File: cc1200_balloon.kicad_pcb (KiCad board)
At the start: 4 copper layers, 50 x 30 mm, 131 parts, among them J101 BATT pads, J201 LoRa ANT pads, J202 SWD+DBG pads, J301 434MHz ANT pads, J401 GNSS ANT pads, J501 BMV080, Q101 DMG3401LSN-7, SW101 PWR, U101 TPS63001, U201 Wio-E5, U301 CC1200, U401 AT6558R-5N32, U501 SCD40-D-R2, U502 AS3935-BQFT, U503 BME688, U504 BME688, X301 40MHz, X401 TCXO 26MHz, X402 32.768kHz

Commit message: Adjust schematic
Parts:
- removed C103, C420, C421: 100n, Capacitor_SMD:C_0402_1005Metric
- removed C105: 10u, Capacitor_SMD:C_0603_1608Metric
- removed C415, C416: 10p, Capacitor_SMD:C_0402_1005Metric
- removed C417, C418, C419: 1u, Capacitor_SMD:C_0402_1005Metric
- removed C422: 100m, cc1200_balloon:SuperCap_KEMET_FCS_D10.7mm
- removed L101: 2.2u, Inductor_SMD:L_1008_2520Metric
- removed R404, R405: 0R, Resistor_SMD:R_0402_1005Metric
- removed U101: TPS63001, Package_SON:VSON-10-1EP_3x3mm_P0.5mm_EP1.65x2.4mm
- added Q102: DMG3401LSN-7, Package_TO_SOT_SMD:SOT-23, F.Cu at (142.4, 111.2)
- C102, C411: value 10u -> 1u; footprint Capacitor_SMD:C_0603_1608Metric -> Capacitor_SMD:C_0402_1005Metric
- C401: value 470p -> 100n
- C402: value 1u -> 100p
- C404, C406: value 100n -> 4u7; footprint Capacitor_SMD:C_0402_1005Metric -> Capacitor_SMD:C_0603_1608Metric
- C405, C412: value 1u -> 100n
- C407, C408, C410: value 100n -> 1u
- C414: value 100p -> 100m; footprint Capacitor_SMD:C_0402_1005Metric -> cc1200_balloon:SuperCap_KEMET_FCS_D10.7mm
- L402: value 4n3 -> 6n8
- R102: value 100R -> 10k
- R402, R403: value 10k -> 22R
- TP401: value GNSS TMS -> GNSS TCK
- TP402: value GNSS TCK -> GNSS TMS
- moved C407 160.7 mm to (235.8, 117.8), turned to 180 degrees
- moved C408 160.2 mm to (235.8, 115.8), turned to 180 degrees
- moved C401 137.0 mm to (255.5, 100.5)
- moved C402 137.0 mm to (255.5, 102.4)
- moved C403 137.0 mm to (255.5, 104.4)
- moved C411 137.0 mm to (247.5, 122.5)
- moved J401 137.0 mm to (214.0, 70.7)
- moved L401 137.0 mm to (230.6, 66.8)
- moved L402 137.0 mm to (230.6, 68.7)
- moved L403 137.0 mm to (247.4, 118.7)
- moved R401 137.0 mm to (230.6, 70.7)
- moved R402 137.0 mm to (230.6, 72.7)
- moved R403 137.0 mm to (230.6, 74.7)
- moved X402 137.0 mm to (243.3, 113.8)
- moved C404 137.0 mm to (247.0, 120.2)
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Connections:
- net /Sensors/AS_ACG renamed Net-(U502-ACG)
- net DBG_TX renamed /MCU/DBG_TX
- net Net-(J201-In) renamed /MCU/LORA_RF
- net Net-(U301-DCPL_PFD_CHP) renamed /CC1200 Radio/CC_DCPL_PFD
- net RADIO_GPIO0 renamed /CC1200 Radio/RADIO_GPIO0
- net RADIO_GPIO3 renamed /CC1200 Radio/RADIO_GPIO3
- net RF_LNAN renamed /CC1200 Radio/RF_LNAN
- net RF_LNAP renamed /CC1200 Radio/RF_LNAP
- net RF_PA renamed /CC1200 Radio/RF_PA
- net RF_TRXSW renamed /CC1200 Radio/RF_TRXSW
- net STATUS_LED renamed /MCU/STATUS_LED
- net SWCLK renamed /MCU/SWCLK
- net SWDIO renamed /MCU/SWDIO
- net XOSC_Q1 renamed /CC1200 Radio/XOSC_Q1
- net XOSC_Q2 renamed /CC1200 Radio/XOSC_Q2
- C102 pad 1: VBATT -> /Power/PWR_GATE
- C102 pad 2: GND -> VBATT
- C104 pad 1: +3V3 -> +BATT
- C106 pad 1: +3V3 -> +BATT
- C201 pad 1: +3V3 -> +BATT
- C202 pad 1: +3V3 -> +BATT
- C203 pad 1: +3V3 -> +BATT
- C301 pad 1: +3V3 -> +BATT
- C302 pad 1: +3V3 -> +BATT
- C303 pad 1: +3V3 -> +BATT
- C304 pad 1: +3V3 -> +BATT
- C305 pad 1: +3V3 -> +BATT
- C306 pad 1: +3V3 -> +BATT
- C307 pad 1: +3V3 -> +BATT
- C308 pad 1: +3V3 -> +BATT
- C309 pad 1: +3V3 -> +BATT
- C310 pad 1: +3V3 -> +BATT
- C311 pad 1: +3V3 -> +BATT
- C312 pad 1: +3V3 -> +BATT
- C320 pad 1: +3V3 -> +BATT
- C401 pad 1: /GNSS/GNSS_ANT_FEED -> /GNSS/GNSS_ANT_BIAS
- C401 pad 2: Net-(C401-Pad2) -> GND
- C402 pad 1: GNSS_ANT_BIAS -> /GNSS/GNSS_ANT_FEED
- C402 pad 2: GND -> Net-(C402-Pad2)
- C403 pad 1: +3V3 -> +BATT
- C404 pad 1: GNSS_VDX -> +BATT
- C405 pad 1: GNSS_AVDD -> +BATT
- C406 pad 1: GNSS_V1P2BB -> /GNSS/GNSS_VCORE
- C407 pad 1: +3V3 -> /GNSS/GNSS_VDD_ANA
- C408 pad 1: +3V3 -> /GNSS/GNSS_VDD12BK
- C409 pad 1: GNSS_V1P2BB -> /GNSS/GNSS_VDD12BB
- C410 pad 1: +3V3 -> /GNSS/GNSS_VDD_PLL
- C411 pad 1: GNSS_VDX -> /GNSS/GNSS_VDD_RF
- C412 pad 1: GNSS_VDD12BK -> /GNSS/GNSS_VX
- C413 pad 1: +3V3 -> /GNSS/GNSS_VBCKP
- C414 pad 1: Net-(X401-OUT) -> /GNSS/GNSS_VBCKP
- C414 pad 2: GNSS_XREF -> GND
- C501 pad 1: +3V3 -> +BATT
- C502 pad 1: +3V3 -> +BATT
- C504 pad 1: +3V3 -> +BATT
- C507 pad 1: +3V3 -> +BATT
- C508 pad 1: +3V3 -> +BATT
- C509 pad 1: +3V3 -> +BATT
- C510 pad 1: +3V3 -> +BATT
- C511 pad 1: +3V3 -> +BATT
- C512 pad 1: +3V3 -> +BATT
- C513 pad 1: +3V3 -> +BATT
- C514 pad 1: +3V3 -> +BATT
- J202 pad 1: +3V3 -> +BATT
- J501 pad 1: +3V3 -> +BATT
- J501 pad 10: +3V3 -> +BATT
- J501 pad 3: +3V3 -> +BATT
- J501 pad 8: +3V3 -> +BATT
- L401 pad 2: GNSS_ANT_BIAS -> /GNSS/GNSS_ANT_BIAS
- L402 pad 1: Net-(C401-Pad2) -> Net-(C402-Pad2)
- L402 pad 2: GNSS_LNA_IN -> /GNSS/GNSS_RF_IN
- L403 pad 1: GNSS_DCDC_SW -> /GNSS/GNSS_DX_SW
- L403 pad 2: GNSS_VDX -> /GNSS/GNSS_VCORE
- R101 pad 1: EN_3V3 -> /Power/PWR_GATE
- R101 pad 2: GND -> VBATT
- R102 pad 1: VBATT -> /Power/SW_ON
- R102 pad 2: /Power/VINA -> /Power/PWR_GATE
- R103 pad 1: VBATT -> +BATT
- R201 pad 1: +3V3 -> +BATT
- R203 pad 1: +3V3 -> +BATT
- R204 pad 1: +3V3 -> +BATT
- R302 pad 1: +3V3 -> +BATT
- R401 pad 1: GNSS_TXD_RAW -> /GNSS/GNSS_TEST
- R401 pad 2: GNSS_TX -> GND
- R402 pad 1: GNSS_RXD_RAW -> /GNSS/GNSS_TXD_RAW
- R402 pad 2: GNSS_RX -> GNSS_TX
- R403 pad 1: GNSS_TEST -> /GNSS/GNSS_RXD_RAW
- R403 pad 2: GND -> GNSS_RX
- SW101 pad 2: EN_3V3 -> /Power/SW_ON
- TP401 pad 1: GNSS_TMS -> /GNSS/GNSS_TCK
- TP402 pad 1: GNSS_TCK -> /GNSS/GNSS_TMS
- U201 pad 1: +3V3 -> +BATT
- U301 pad 1: +3V3 -> +BATT
- U301 pad 12: +3V3 -> +BATT
- U301 pad 13: +3V3 -> +BATT
- U301 pad 15: +3V3 -> +BATT
- U301 pad 22: +3V3 -> +BATT
- U301 pad 25: +3V3 -> +BATT
- U301 pad 27: +3V3 -> +BATT
- U301 pad 28: +3V3 -> +BATT
- U301 pad 5: +3V3 -> +BATT
- U401 pad 1: GNSS_LNA_IN -> /GNSS/GNSS_VDD_ANA
- U401 pad 10: unconnected-(U401-GPIO9-Pad10) -> /GNSS/GNSS_ANT_BIAS
- U401 pad 11: unconnected-(U401-GPIO2/SCL-Pad11) -> /GNSS/GNSS_RTC_O
- U401 pad 12: unconnected-(U401-GPIO3/SDA-Pad12) -> /GNSS/GNSS_RTC_I
- U401 pad 13: GNSS_V1P2BB -> unconnected-(U401-GPIO4/TXD1-Pad13)
- U401 pad 14: +3V3 -> unconnected-(U401-GPIO5/RXD1-Pad14)
- U401 pad 15: unconnected-(U401-GPIO4/TXD2-Pad15) -> /GNSS/GNSS_TCK
- U401 pad 16: unconnected-(U401-GPIO5/RXD2-Pad16) -> /GNSS/GNSS_TMS
- U401 pad 17: GNSS_TMS -> unconnected-(U401-nRST-Pad17)
- U401 pad 18: GNSS_TCK -> /GNSS/GNSS_RXD_RAW
- U401 pad 19: GNSS_TXD_RAW -> /GNSS/GNSS_TXD_RAW
- U401 pad 2: GNSS_ANT_BIAS -> /GNSS/GNSS_VX
- U401 pad 20: GNSS_RXD_RAW -> unconnected-(U401-GPIO6-Pad20)
- U401 pad 21: GNSS_PPS -> +BATT
- U401 pad 22: +3V3 -> /GNSS/GNSS_DX_SW
- U401 pad 23: NRST -> /GNSS/GNSS_VCORE
- U401 pad 24: GNSS_V1P2BB -> /GNSS/GNSS_VDD12BB
- U401 pad 25: GNSS_VDX -> unconnected-(U401-NC-Pad25)
- U401 pad 26: GNSS_DCDC_SW -> unconnected-(U401-NC-Pad26)
- U401 pad 27: +3V3 -> unconnected-(U401-NC-Pad27)
- U401 pad 28: GNSS_TEST -> unconnected-(U401-NC-Pad28)
- U401 pad 29: GNSS_ONOFF -> /GNSS/GNSS_TEST
- U401 pad 3: +3V3 -> /GNSS/GNSS_XREF
- U401 pad 30: GNSS_XREF -> GNSS_ONOFF
- U401 pad 31: GNSS_VBK -> unconnected-(U401-GPIO10/SCL-Pad31)
- U401 pad 32: GNSS_VDD12BK -> unconnected-(U401-GPIO11/SDA-Pad32)
- U401 pad 33: GNSS_RTC_XO -> unconnected-(U401-GPIO16-Pad33)
- U401 pad 34: GNSS_RTC_XI -> unconnected-(U401-GPIO12-Pad34)
- U401 pad 35: GNSS_VDX -> GNSS_PPS
- U401 pad 36: GNSS_DVDD -> unconnected-(U401-GPIO14-Pad36)
- U401 pad 37: GNSS_VDD_PLL -> unconnected-(U401-GPIO15-Pad37)
- U401 pad 38: unconnected-(U401-RFA_IN-Pad38) -> /GNSS/GNSS_VDD_PLL
- U401 pad 39: GNSS_VDD_RF -> /GNSS/GNSS_VDD_RF
- U401 pad 4: GNSS_VDX -> unconnected-(U401-TST_RF-Pad4)
- U401 pad 40: unconnected-(U401-LNA_OUT-Pad40) -> /GNSS/GNSS_RF_IN
- U401 pad 5: unconnected-(U401-TST_ANA-Pad5) -> /GNSS/GNSS_VDD12BK
- U401 pad 6: GNSS_AVDD -> /GNSS/GNSS_VBCKP
- U401 pad 7: unconnected-(U401-TST_DIG-Pad7) -> +BATT
- U501 pad 19: +3V3 -> +BATT
- U501 pad 7: +3V3 -> +BATT
- U502 pad 15: +3V3 -> +BATT
- U502 pad 16: +3V3 -> +BATT
- U502 pad 5: +3V3 -> +BATT
- U502 pad 6: +3V3 -> +BATT
- U502 pad 8: +3V3 -> +BATT
- U502 pad 9: +3V3 -> +BATT
- U503 pad 2: +3V3 -> +BATT
- U503 pad 6: +3V3 -> +BATT
- U503 pad 8: +3V3 -> +BATT
- U504 pad 2: +3V3 -> +BATT
- U504 pad 5: +3V3 -> +BATT
- U504 pad 6: +3V3 -> +BATT
- U504 pad 8: +3V3 -> +BATT
- X401 pad 1: Net-(X401-Tri-State) -> /GNSS/GNSS_VX
- X401 pad 3: Net-(X401-OUT) -> /GNSS/GNSS_XREF
- X401 pad 4: +3V3 -> /GNSS/GNSS_VX
- X402 pad 1: GNSS_RTC_XI -> /GNSS/GNSS_RTC_I
- X402 pad 2: GNSS_RTC_XO -> /GNSS/GNSS_RTC_O
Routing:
- added copper zone on In2.Cu, net +BATT
- removed copper zone on In2.Cu, net +3V3

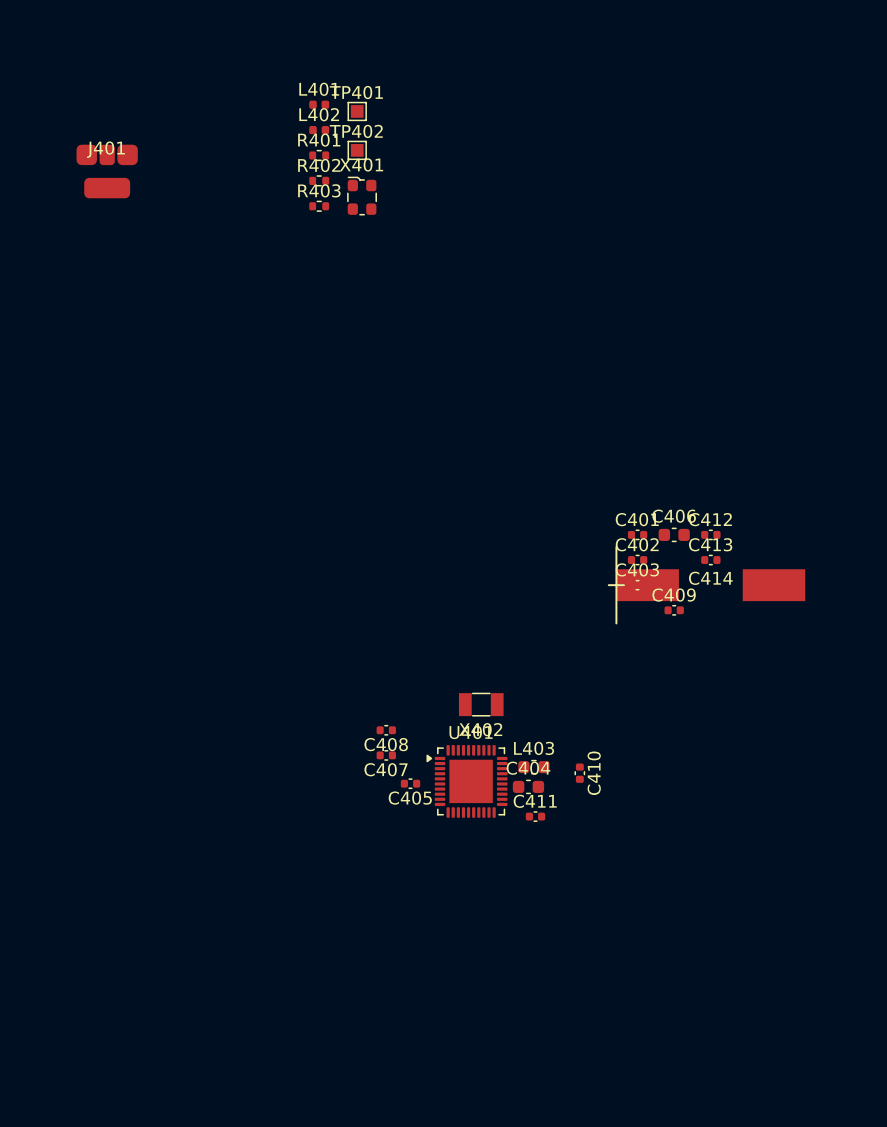
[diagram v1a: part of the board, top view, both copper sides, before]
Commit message: Update schematic wiring
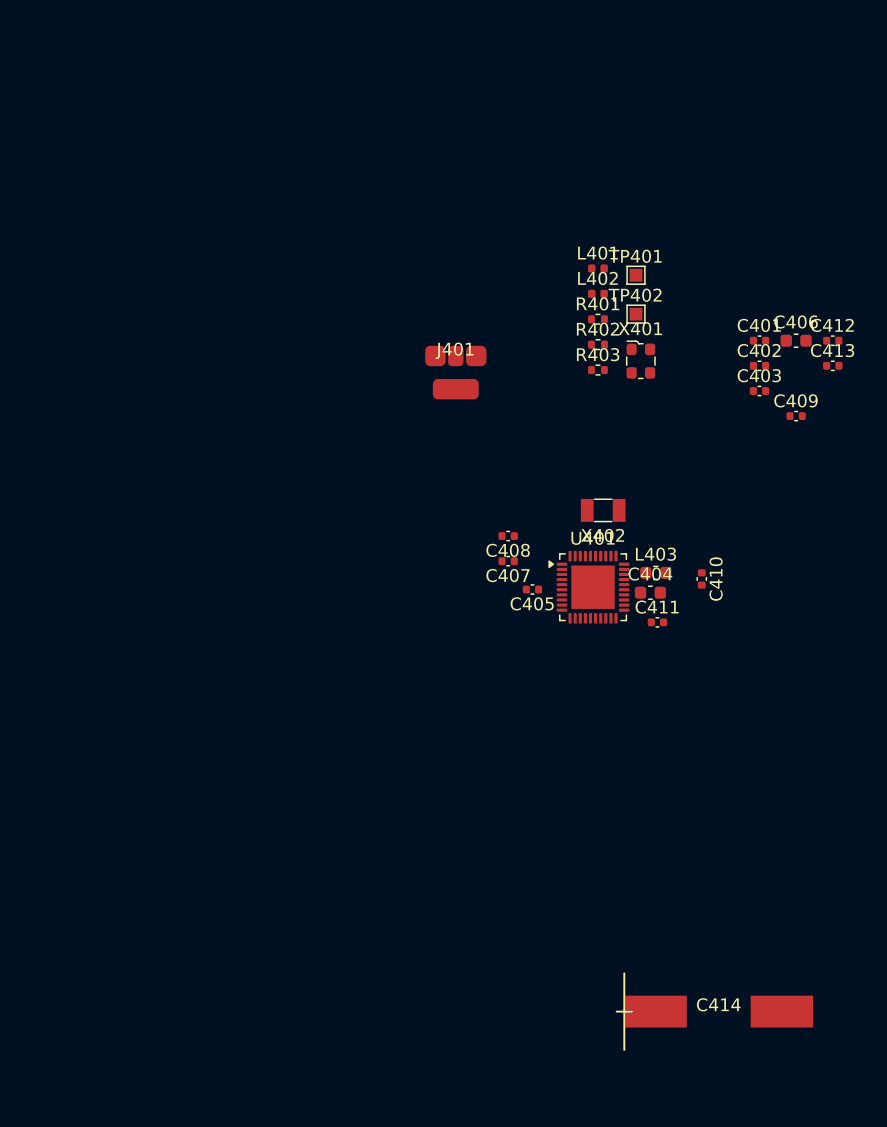
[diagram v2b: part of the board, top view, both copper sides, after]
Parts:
- moved C414 33.4 mm to (261.9, 137.8)
- moved J401 31.5 mm to (241.3, 86.5)
- moved X401 25.3 mm to (255.8, 86.8)
- moved L401 25.3 mm to (252.4, 79.6)
- moved R402 25.3 mm to (252.4, 85.6)
- moved TP401 25.3 mm to (255.4, 80.1)
- moved TP402 25.3 mm to (255.4, 83.2)
- moved L402 25.3 mm to (252.4, 81.6)
- moved R401 25.3 mm to (252.4, 83.6)
- moved R403 25.3 mm to (252.4, 87.5)
- moved C401 18.0 mm to (265.1, 85.2)
- moved C402 18.0 mm to (265.1, 87.2)
- moved C403 18.0 mm to (265.1, 89.2)
- moved C411 18.0 mm to (257.1, 107.3)
- moved L403 18.0 mm to (257.0, 103.5)
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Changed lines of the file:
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@@
 	(footprint "cc1200_balloon:AT6558R_QFN-40-1EP_5x5mm_P0.4mm_EP3.4x3.4mm"
 		(layer "F.Cu")
-		(at 242.5 119.79)
+		(at 252.055 104.57)
 		(descr "QFN, 40 pin, 5x5mm body, 0.4mm pitch, 3.4x3.4mm thermal pad (ZHONGKEWEI AT6558R data sheet section 8.2)")
 		(tags "QFN NoLead")
@@
 	(footprint "Inductor_SMD:L_0603_1608Metric"
 		(layer "F.Cu")
-		(at 247.42 118.67)
+		(at 256.975 103.45)
 		(descr "Inductor SMD 0603 (1608 Metric), square (rectangular) end terminal, IPC-7351 nominal, (Body size source: http://www.tortai-tech.com/upload/download/2011102023233369053.pdf)")
 		(tags "inductor")
@@
 	(footprint "Inductor_SMD:L_0402_1005Metric"
 		(layer "F.Cu")
-		(at 230.5925 66.755)
+		(at 252.44 79.59)
 		(descr "Inductor SMD 0402 (1005 Metric), square (rectangular) end terminal, IPC-7351 nominal, (Body size source: http://www.tortai-tech.com/upload/download/2011102023233369053.pdf)")
 		(tags "inductor")
@@
 	(footprint "cc1200_balloon:SuperCap_KEMET_FCS_D10.7mm"
 		(layer "F.Cu")
-		(at 261.285 104.41)
+		(at 261.905 137.83)
 		(descr "KEMET FC/FCS series supercapacitor, 10.7mm diameter SMD can, 5.5mm high; pad 1 is positive")
 		(tags "supercapacitor EDLC backup KEMET")
@@
 	(footprint "Capacitor_SMD:C_0402_1005Metric"
 		(layer "F.Cu")
-		(at 258.415 106.38)
+		(at 267.97 91.16)
 		(descr "Capacitor SMD 0402 (1005 Metric), square (rectangular) end terminal, IPC-7351 nominal, (Body size source: IPC-SM-782 page 76, https://www.pcb-3d.com/wordpress/wp-content/uploads/ipc-sm-782a_amendment_1_and_2.pdf)")
 		(tags "capacitor")
@@
 	(footprint "TestPoint:TestPoint_Pad_1.0x1.0mm"
 		(layer "F.Cu")
-		(at 233.5725 67.285)
+		(at 255.42 80.12)
 		(descr "SMD rectangular pad as test Point, square 1.0mm side length")
 		(tags "test point SMD pad rectangle square")
@@
 	(footprint "Capacitor_SMD:C_0402_1005Metric"
 		(layer "F.Cu")
-		(at 255.545 100.47)
+		(at 265.1 85.25)
 		(descr "Capacitor SMD 0402 (1005 Metric), square (rectangular) end terminal, IPC-7351 nominal, (Body size source: IPC-SM-782 page 76, https://www.pcb-3d.com/wordpress/wp-content/uploads/ipc-sm-782a_amendment_1_and_2.pdf)")
 		(tags "capacitor")
@@
 	(footprint "Capacitor_SMD:C_0402_1005Metric"
 		(layer "F.Cu")
-		(at 261.285 100.47)
+		(at 270.84 85.25)
 		(descr "Capacitor SMD 0402 (1005 Metric), square (rectangular) end terminal, IPC-7351 nominal, (Body size source: IPC-SM-782 page 76, https://www.pcb-3d.com/wordpress/wp-content/uploads/ipc-sm-782a_amendment_1_and_2.pdf)")
 		(tags "capacitor")
@@
 	(footprint "Capacitor_SMD:C_0402_1005Metric"
 		(layer "F.Cu")
-		(at 235.85 117.75 180)
+		(at 245.405 102.53 180)
 		(descr "Capacitor SMD 0402 (1005 Metric), square (rectangular) end terminal, IPC-7351 nominal, (Body size source: IPC-SM-782 page 76, https://www.pcb-3d.com/wordpress/wp-content/uploads/ipc-sm-782a_amendment_1_and_2.pdf)")
 		(tags "capacitor")
@@
 	(footprint "Capacitor_SMD:C_0603_1608Metric"
 		(layer "F.Cu")
-		(at 246.995 120.22)
+		(at 256.55 105)
 		(descr "Capacitor SMD 0603 (1608 Metric), square (rectangular) end terminal, IPC-7351 nominal, (Body size source: IPC-SM-782 page 76, https://www.pcb-3d.com/wordpress/wp-content/uploads/ipc-sm-782a_amendment_1_and_2.pdf)")
 		(tags "capacitor")
@@
 	(footprint "Capacitor_SMD:C_0402_1005Metric"
 		(layer "F.Cu")
-		(at 261.285 102.44)
+		(at 270.84 87.22)
 		(descr "Capacitor SMD 0402 (1005 Metric), square (rectangular) end terminal, IPC-7351 nominal, (Body size source: IPC-SM-782 page 76, https://www.pcb-3d.com/wordpress/wp-content/uploads/ipc-sm-782a_amendment_1_and_2.pdf)")
 		(tags "capacitor")
@@
 	(footprint "Crystal:Crystal_SMD_3215-2Pin_3.2x1.5mm"
 		(layer "F.Cu")
-		(at 243.295 113.77 180)
+		(at 252.85 98.55 180)
 		(descr "SMD Crystal FC-135 https://support.epson.biz/td/api/doc_check.php?dl=brief_FC-135R_en.pdf")
 		(tags "SMD SMT Crystal")
@@
 	(footprint "Resistor_SMD:R_0402_1005Metric"
 		(layer "F.Cu")
-		(at 230.5925 74.715)
+		(at 252.44 87.55)
 		(descr "Resistor SMD 0402 (1005 Metric), square (rectangular) end terminal, IPC-7351 nominal, (Body size source: IPC-SM-782 page 72, https://www.pcb-3d.com/wordpress/wp-content/uploads/ipc-sm-782a_amendment_1_and_2.pdf)")
 		(tags "resistor")
@@
 	(footprint "cc1200_balloon:SolderPad_Coax_Pigtail"
 		(layer "F.Cu")
-		(at 213.9775 70.69)
+		(at 241.3 86.45)
 		(descr "Coax pigtail solder pads: centre conductor, coplanar grounds and a braid pad; replaces an SMA or u.FL connector")
 		(tags "solder pad coax pigtail RF antenna")
@@
 	(footprint "Capacitor_SMD:C_0603_1608Metric"
 		(layer "F.Cu")
-		(at 258.415 100.47)
+		(at 267.97 85.25)
 		(descr "Capacitor SMD 0603 (1608 Metric), square (rectangular) end terminal, IPC-7351 nominal, (Body size source: IPC-SM-782 page 76, https://www.pcb-3d.com/wordpress/wp-content/uploads/ipc-sm-782a_amendment_1_and_2.pdf)")
 		(tags "capacitor")
@@
 	(footprint "Capacitor_SMD:C_0402_1005Metric"
 		(layer "F.Cu")
-		(at 255.545 102.44)
+		(at 265.1 87.22)
 		(descr "Capacitor SMD 0402 (1005 Metric), square (rectangular) end terminal, IPC-7351 nominal, (Body size source: IPC-SM-782 page 76, https://www.pcb-3d.com/wordpress/wp-content/uploads/ipc-sm-782a_amendment_1_and_2.pdf)")
 		(tags "capacitor")
@@
 	(footprint "Capacitor_SMD:C_0402_1005Metric"
 		(layer "F.Cu")
-		(at 251.02 119.145 -90)
+		(at 260.575 103.925 -90)
 		(descr "Capacitor SMD 0402 (1005 Metric), square (rectangular) end terminal, IPC-7351 nominal, (Body size source: IPC-SM-782 page 76, https://www.pcb-3d.com/wordpress/wp-content/uploads/ipc-sm-782a_amendment_1_and_2.pdf)")
 		(tags "capacitor")
@@
 	(footprint "Oscillator:Oscillator_SMD_ECS_2520MV-xxx-xx-4Pin_2.5x2.0mm"
 		(layer "F.Cu")
-		(at 233.9525 74.015)
+		(at 255.8 86.85)
 		(descr "Miniature Crystal Clock Oscillator ECS 2520MV series, https://www.ecsxtal.com/store/pdf/ECS-2520MV.pdf")
 		(tags "Miniature Crystal Clock Oscillator ECS 2520MV series SMD SMT HCMOS")
@@
 	(footprint "Resistor_SMD:R_0402_1005Metric"
 		(layer "F.Cu")
-		(at 230.5925 72.725)
+		(at 252.44 85.56)
 		(descr "Resistor SMD 0402 (1005 Metric), square (rectangular) end terminal, IPC-7351 nominal, (Body size source: IPC-SM-782 page 72, https://www.pcb-3d.com/wordpress/wp-content/uploads/ipc-sm-782a_amendment_1_and_2.pdf)")
 		(tags "resistor")
@@
 	(footprint "Capacitor_SMD:C_0402_1005Metric"
 		(layer "F.Cu")
-		(at 237.75 119.97 180)
+		(at 247.305 104.75 180)
 		(descr "Capacitor SMD 0402 (1005 Metric), square (rectangular) end terminal, IPC-7351 nominal, (Body size source: IPC-SM-782 page 76, https://www.pcb-3d.com/wordpress/wp-content/uploads/ipc-sm-782a_amendment_1_and_2.pdf)")
 		(tags "capacitor")
@@
 	(footprint "Capacitor_SMD:C_0402_1005Metric"
 		(layer "F.Cu")
-		(at 255.545 104.41)
+		(at 265.1 89.19)
 		(descr "Capacitor SMD 0402 (1005 Metric), square (rectangular) end terminal, IPC-7351 nominal, (Body size source: IPC-SM-782 page 76, https://www.pcb-3d.com/wordpress/wp-content/uploads/ipc-sm-782a_amendment_1_and_2.pdf)")
 		(tags "capacitor")
@@
 	(footprint "Inductor_SMD:L_0402_1005Metric"
 		(layer "F.Cu")
-		(at 230.5925 68.745)
+		(at 252.44 81.58)
 		(descr "Inductor SMD 0402 (1005 Metric), square (rectangular) end terminal, IPC-7351 nominal, (Body size source: http://www.tortai-tech.com/upload/download/2011102023233369053.pdf)")
 		(tags "inductor")
@@
 	(footprint "Capacitor_SMD:C_0402_1005Metric"
 		(layer "F.Cu")
-		(at 235.85 115.78 180)
+		(at 245.405 100.56 180)
 		(descr "Capacitor SMD 0402 (1005 Metric), square (rectangular) end terminal, IPC-7351 nominal, (Body size source: IPC-SM-782 page 76, https://www.pcb-3d.com/wordpress/wp-content/uploads/ipc-sm-782a_amendment_1_and_2.pdf)")
 		(tags "capacitor")
@@
 	(footprint "Capacitor_SMD:C_0402_1005Metric"
 		(layer "F.Cu")
-		(at 247.545 122.545)
+		(at 257.1 107.325)
 		(descr "Capacitor SMD 0402 (1005 Metric), square (rectangular) end terminal, IPC-7351 nominal, (Body size source: IPC-SM-782 page 76, https://www.pcb-3d.com/wordpress/wp-content/uploads/ipc-sm-782a_amendment_1_and_2.pdf)")
 		(tags "capacitor")
@@
 	(footprint "TestPoint:TestPoint_Pad_1.0x1.0mm"
 		(layer "F.Cu")
-		(at 233.5725 70.335)
+		(at 255.42 83.17)
 		(descr "SMD rectangular pad as test Point, square 1.0mm side length")
 		(tags "test point SMD pad rectangle square")
@@
 	(footprint "Resistor_SMD:R_0402_1005Metric"
 		(layer "F.Cu")
-		(at 230.5925 70.735)
+		(at 252.44 83.57)
 		(descr "Resistor SMD 0402 (1005 Metric), square (rectangular) end terminal, IPC-7351 nominal, (Body size source: IPC-SM-782 page 72, https://www.pcb-3d.com/wordpress/wp-content/uploads/ipc-sm-782a_amendment_1_and_2.pdf)")
 		(tags "resistor")

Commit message: Adjust layout and schematic
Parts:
- removed C414: 100m, cc1200_balloon:SuperCap_KEMET_FCS_D10.7mm
- J401: value GNSS ANT pads -> GNSS ANT
- moved C413 87.8 mm to (183.2, 93.8), turned to 180 degrees
- moved C412 87.8 mm to (183.2, 91.8), turned to 180 degrees
- moved C402 79.9 mm to (185.2, 86.6), turned to 180 degrees
- moved C401 77.6 mm to (187.5, 84.3)
- moved C409 76.0 mm to (192.0, 93.7)
- moved C410 75.5 mm to (186.8, 88.3), turned to 90 degrees
- moved C403 73.9 mm to (191.7, 97.7)
- moved C411 73.9 mm to (185.7, 88.3), turned to 90 degrees
- moved C406 73.7 mm to (194.8, 93.2)
- moved X401 73.5 mm to (182.3, 87.8)
- moved L402 68.1 mm to (184.7, 88.3), turned to -90 degrees
- moved X402 67.4 mm to (185.4, 98.1), turned to 0 degrees
- moved L401 66.8 mm to (185.8, 84.8), turned to 90 degrees
- moved U401 65.3 mm to (187.8, 93.4)
- moved L403 65.0 mm to (192.6, 94.9)
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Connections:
- net /GNSS/GNSS_ANT_FEED renamed /GNSS/GNSS_ANT
